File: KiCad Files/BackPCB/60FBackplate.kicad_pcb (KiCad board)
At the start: 2 copper layers, 283 x 126.5 mm, 10 parts

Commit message: adjusted designs and generated gerbers
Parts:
- added kibuzzard-62DEDAB9: G***, kibuzzard-62DEDAB9, B.Cu at (218.6, 97.6)

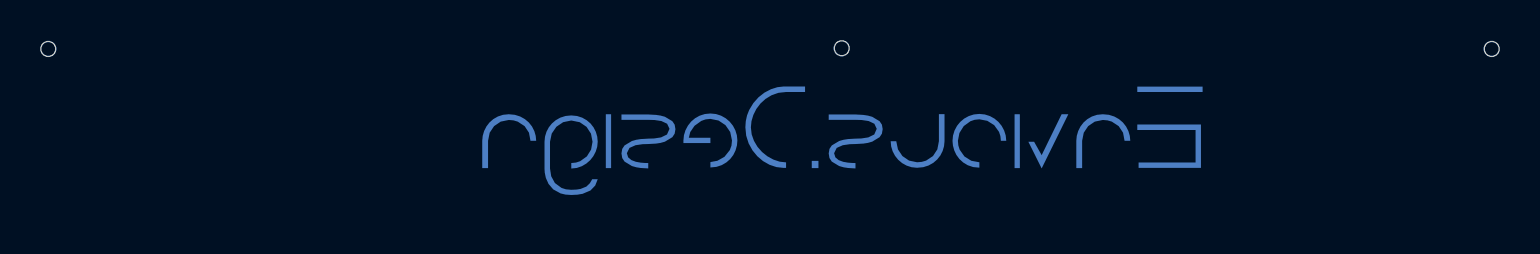
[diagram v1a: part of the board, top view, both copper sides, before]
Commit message: Corrected mount hole parity between mainPCB MX and Backplate.
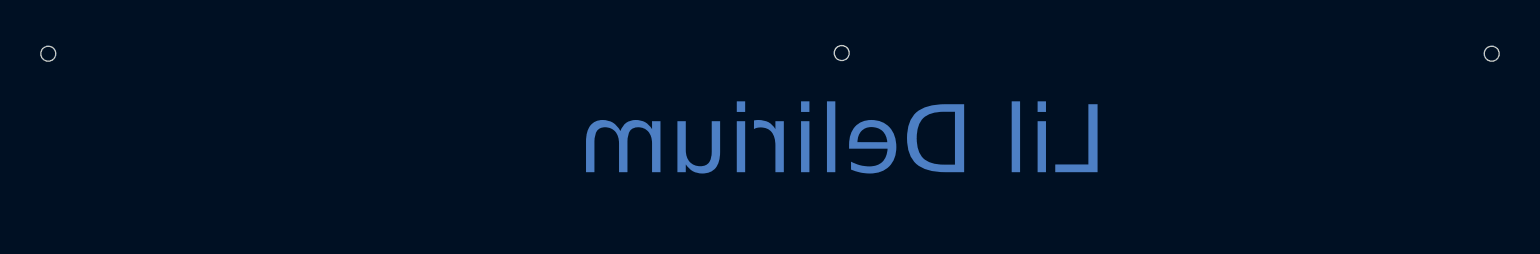
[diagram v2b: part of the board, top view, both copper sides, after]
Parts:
- removed kibuzzard-62DEDAB9 (x2): G***, kibuzzard-62DEDAB9
- moved H10 0.70 mm to (314.1, 84.8)
- moved H4 0.70 mm to (101.8, 84.8)
- moved H9 0.70 mm to (218.5, 84.7)
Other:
- board text added: "Lil Delirium"
- board text added: "https://github.com/Envious-Data/Env-KB60F Version: 2.0"
- board text removed: "https://github.com/Envious-Data/Env-KB60F Version: 1.0"
